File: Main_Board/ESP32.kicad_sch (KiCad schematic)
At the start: 11 parts, among them J1 RESET, J2 MAIN_UART, U1 ESP32-S3-MINI-1U

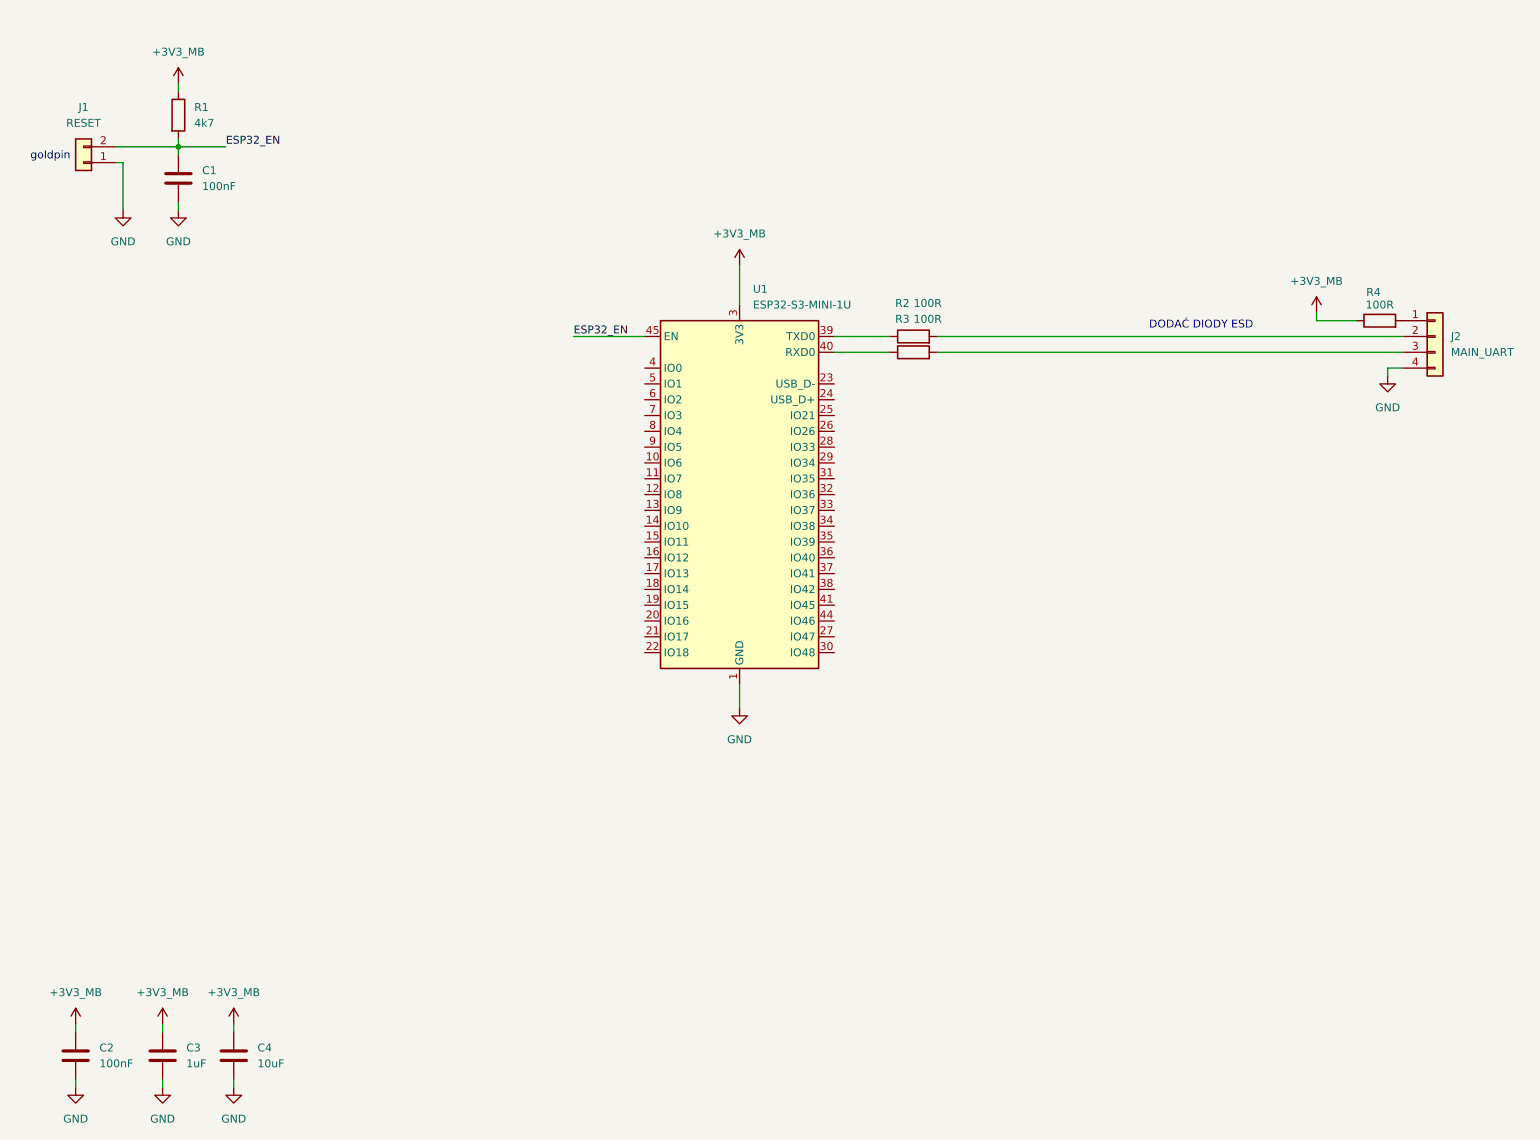
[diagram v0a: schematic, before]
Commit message: PSU Ready + ESP32 advanced
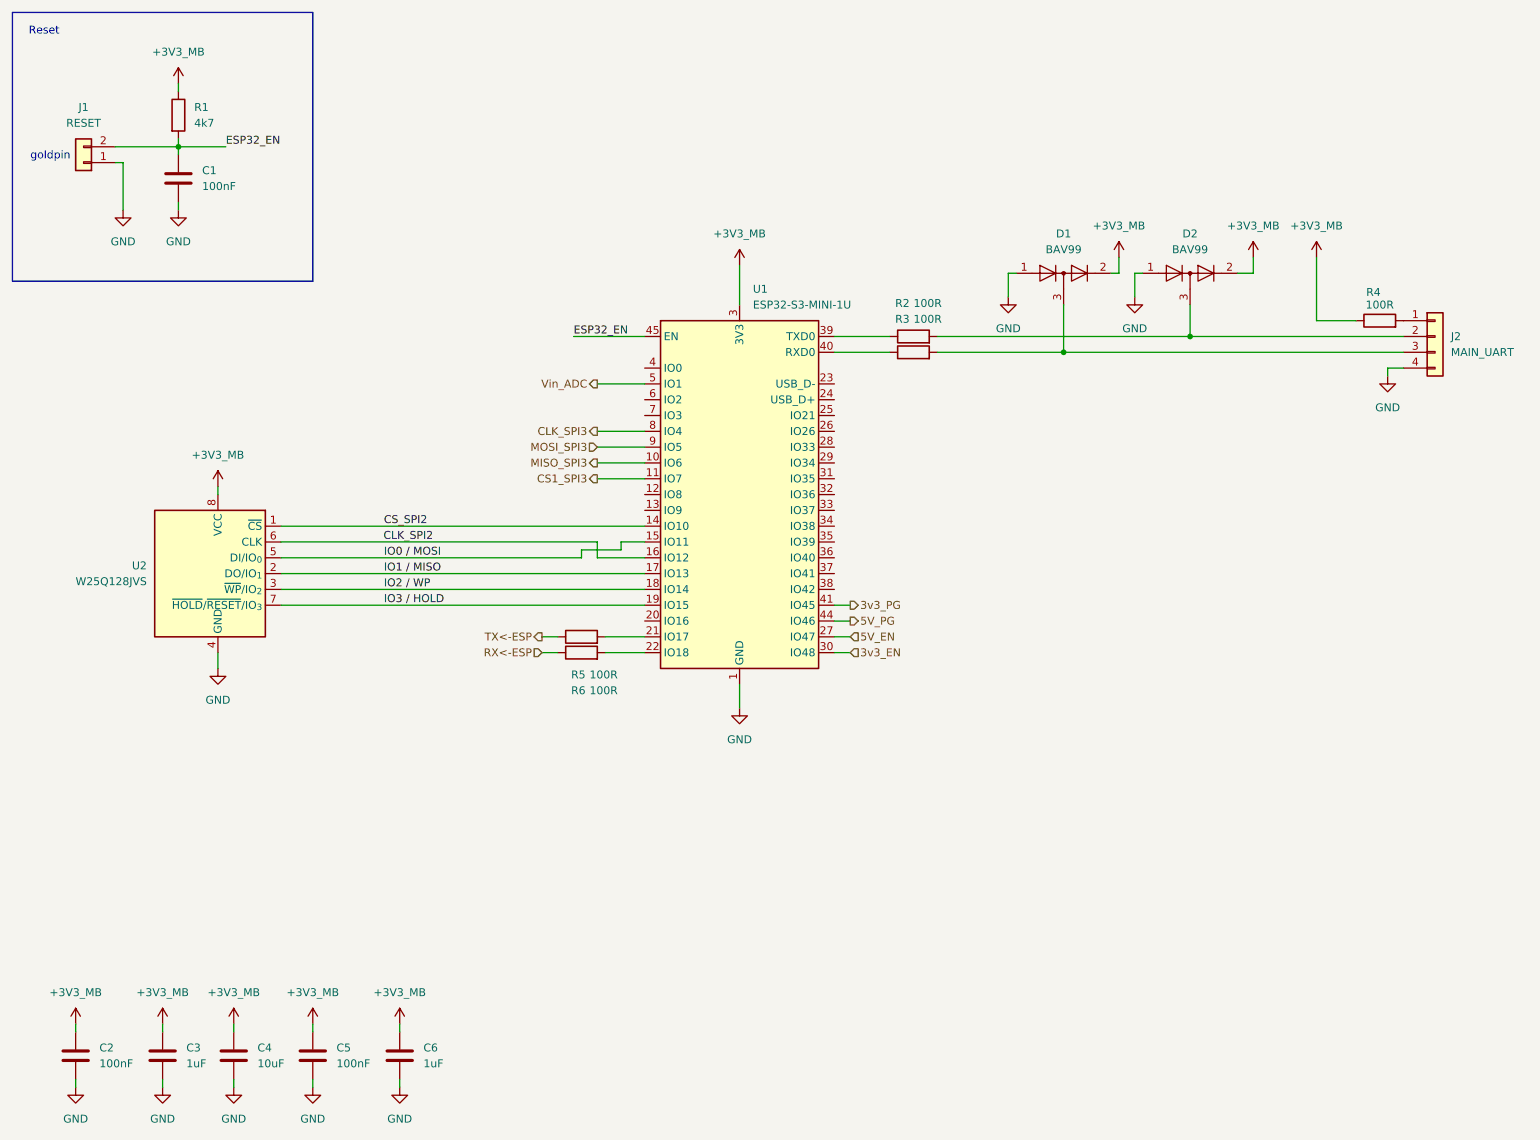
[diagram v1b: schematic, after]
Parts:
- added C5: 100nF, symbol Device:C
- added C6: 1uF, symbol Device:C
- added D1, D2: BAV99, Package_TO_SOT_SMD:SOT-23, symbol Diode:BAV99
- added R5, R6: 100R, symbol Device:R
- added U2: W25Q128JVS, Package_SO:SOIC-8_5.3x5.3mm_P1.27mm, symbol Memory_Flash:W25Q128JVS
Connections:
- net +3V3_MB: now also C5.1, C6.1, D1.2 (A), D2.2 (A), U2.8 (VCC)
- net GND: now also C5.2, C6.2, D1.1 (K), D2.1 (K), U2.4 (GND)
- net at J2.2 (Pin_2), R2.2: now also D2.3 (K)
- net MISO_SPI3: now reaches U1.10 (IO6)
- net CS1_SPI3: now reaches U1.11 (IO7)
- net CS_SPI2: now reaches U1.14 (IO10)
- net CS_SPI2: now also U2.1 (~{CS})
- net IO0 / MOSI: now reaches U1.15 (IO11)
- net IO0 / MOSI: now also U2.5 (DI/IO_{0})
- net CLK_SPI2: now reaches U1.16 (IO12)
- net CLK_SPI2: now also U2.6 (CLK)
- net IO1 / MISO: now reaches U1.17 (IO13)
- net IO1 / MISO: now also U2.2 (DO/IO_{1})
- net IO2 / WP: now reaches U1.18 (IO14)
- net IO2 / WP: now also U2.3 (~{WP}/IO_{2})
- net IO3 / HOLD: now reaches U1.19 (IO15)
- net IO3 / HOLD: now also U2.7 (~{HOLD}/~{RESET}/IO_{3})
- net at U1.21 (IO17): now also R5.2
- net at U1.22 (IO18): now also R6.2
- net 5V_EN: now reaches U1.27 (IO47)
- net 3v3_EN: now reaches U1.30 (IO48)
- net 3v3_PG: now reaches U1.41 (IO45)
- net 5V_PG: now reaches U1.44 (IO46)
- net Vin_ADC: now reaches U1.5 (IO1)
- net CLK_SPI3: now reaches U1.8 (IO4)
- net MOSI_SPI3: now reaches U1.9 (IO5)
- net at J2.3 (Pin_3), R3.2: now also D1.3 (K)
- new net RX<-ESP: R6.1
- new net TX<-ESP: R5.1
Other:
- note added: "Reset"
- note removed: "DODAĆ DIODY ESD"

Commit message: Input Protection
Irlm is left to be calculated
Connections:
- no-connect marks 0 -> 2
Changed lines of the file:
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@@
 		(color 0 0 0 0)
+	)
+	(no_connect
+		(at 146.05 77.47)
+	)
+	(no_connect
+		(at 146.05 74.93)
 	)
 	(wire

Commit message: RS485 Transciever + Input Protection fix
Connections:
- net RSDIR: now reaches U1.25 (IO21)
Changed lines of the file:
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@@
+	(wire
+		(pts
+			(xy 148.59 80.01) (xy 146.05 80.01)
+		)
+		(stroke
+			(width 0)
+			(type default)
+		)
+	)
 	(wire
 		(pts
@@
 		(effects
 			(font
+				(size 1.27 1.27)
+			)
+			(justify left)
+		)
+	)
+	(hierarchical_label "RSDIR"
+		(shape input)
+		(at 148.59 80.01 0)
+		(effects
+			(font

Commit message: Aesthetics/cleanup
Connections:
- net RSDIR renamed MODULE_BUS_DIR
- net RX<-ESP renamed MODULE_BUS_RX
- net TX<-ESP renamed MODULE_BUS_TX
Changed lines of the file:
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@@
 		)
 	)
-	(hierarchical_label "RSDIR"
+	(hierarchical_label "MODULE_BUS_DIR"
 		(shape input)
 		(at 148.59 80.01 0)
@@
 		)
 	)
-	(hierarchical_label "RX<-ESP"
+	(hierarchical_label "MODULE_BUS_RX"
 		(shape input)
 		(at 99.06 118.11 180)
@@
 		)
 	)
-	(hierarchical_label "TX<-ESP"
+	(hierarchical_label "MODULE_BUS_TX"
 		(shape output)
 		(at 99.06 115.57 180)

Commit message: add external obrds interfaces
Todo pyro chanells
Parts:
- added Q1: 2N7002, Package_TO_SOT_SMD:SOT-23, symbol Transistor_FET:2N7002
- added R32: 4k7, symbol Device:R
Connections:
- net ESP32_EN: now also Q1.3 (D)
- net GND: now also Q1.2 (S), R32.2
- net MODULE_BUS_DIR: now also U1.20 (IO16); no longer U1.25 (IO21)
- new net RST: Q1.1 (G), R32.1
- new net SYNC: U1.25 (IO21)

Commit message: Add buzzer, Add LED, ADD R&D jumper
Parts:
- added R5, R6, R7, R8: 100R, symbol Device:R
- renumbered C2 to C1, C3 to C2, C1 to C3, R32 to R1, R3 to R10, R4 to R11, R1 to R2, R5 to R3, R6 to R4, R2 to R9, U2 to U1, U1 to U2
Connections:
- net at U2.35 (IO39): now also R5.1
- net at U2.36 (IO40): now also R6.1
- net at U2.37 (IO41): now also R7.1
- net at U2.38 (IO42): now also R8.1
- new net BUZZER: R6.2
- new net LED: R5.2
- new net Piro1: R7.2
- new net Piro2: R8.2

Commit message: ADD footprints
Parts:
- C1, C2, C3, C4, C5, C6: footprint (none) -> Capacitor_SMD:C_0603_1608Metric
- J1: footprint (none) -> Connector_PinHeader_2.54mm:PinHeader_1x02_P2.54mm_Vertical
- J2: footprint (none) -> Connector_PinHeader_2.54mm:PinHeader_1x04_P2.54mm_Horizontal
- R1, R10, R11, R2, R3, R4, R5, R6, R7, R8, R9: footprint (none) -> Resistor_SMD:R_0603_1608Metric
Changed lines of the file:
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@@
 			)
 		)
-		(property "Footprint" ""
+		(property "Footprint" "Resistor_SMD:R_0603_1608Metric"
 			(at 233.68 66.548 90)
 			(hide yes)
@@
 			)
 		)
-		(property "Footprint" ""
+		(property "Footprint" "Capacitor_SMD:C_0603_1608Metric"
 			(at 41.6052 45.72 0)
 			(hide yes)
@@
 			)
 		)
-		(property "Footprint" ""
+		(property "Footprint" "Resistor_SMD:R_0603_1608Metric"
 			(at 38.862 31.75 90)
 			(hide yes)
@@
 			)
 		)
-		(property "Footprint" ""
+		(property "Footprint" "Resistor_SMD:R_0603_1608Metric"
 			(at 158.75 69.088 90)
 			(hide yes)
@@
 			)
 		)
-		(property "Footprint" ""
+		(property "Footprint" "Capacitor_SMD:C_0603_1608Metric"
 			(at 50.4952 186.69 0)
 			(hide yes)
@@
 			)
 		)
-		(property "Footprint" ""
+		(property "Footprint" "Resistor_SMD:R_0603_1608Metric"
 			(at 23.622 66.04 90)
 			(hide yes)
@@
 			)
 		)
-		(property "Footprint" ""
+		(property "Footprint" "Capacitor_SMD:C_0603_1608Metric"
 			(at 25.0952 186.69 0)
 			(hide yes)
@@
 			)
 		)
-		(property "Footprint" ""
+		(property "Footprint" "Capacitor_SMD:C_0603_1608Metric"
 			(at 77.1652 186.69 0)
 			(hide yes)
@@
 			)
 		)
-		(property "Footprint" ""
+		(property "Footprint" "Resistor_SMD:R_0603_1608Metric"
 			(at 105.41 119.888 90)
 			(hide yes)
@@
 			)
 		)
-		(property "Footprint" ""
+		(property "Footprint" "Resistor_SMD:R_0603_1608Metric"
 			(at 152.4 104.648 90)
 			(hide yes)
@@
 			)
 		)
-		(property "Footprint" ""
+		(property "Footprint" "Resistor_SMD:R_0603_1608Metric"
 			(at 152.4 107.188 90)
 			(hide yes)
@@
 			)
 		)
-		(property "Footprint" ""
+		(property "Footprint" "Resistor_SMD:R_0603_1608Metric"
 			(at 152.4 109.728 90)
 			(hide yes)
@@
 			)
 		)
-		(property "Footprint" ""
+		(property "Footprint" "Resistor_SMD:R_0603_1608Metric"
 			(at 105.41 117.348 90)
 			(hide yes)
@@
 			)
 		)
-		(property "Footprint" ""
+		(property "Footprint" "Capacitor_SMD:C_0603_1608Metric"
 			(at 39.0652 186.69 0)
 			(hide yes)
@@
 			)
 		)
-		(property "Footprint" ""
+		(property "Footprint" "Resistor_SMD:R_0603_1608Metric"
 			(at 152.4 102.108 90)
 			(hide yes)
@@
 			)
 		)
-		(property "Footprint" ""
+		(property "Footprint" "Connector_PinHeader_2.54mm:PinHeader_1x02_P2.54mm_Vertical"
 			(at 25.4 39.37 0)
 			(hide yes)
@@
 			)
 		)
-		(property "Footprint" ""
+		(property "Footprint" "Connector_PinHeader_2.54mm:PinHeader_1x04_P2.54mm_Horizontal"
 			(at 242.57 67.31 0)
 			(hide yes)
@@
 			)
 		)
-		(property "Footprint" ""
+		(property "Footprint" "Resistor_SMD:R_0603_1608Metric"
 			(at 158.75 71.628 90)
 			(hide yes)
@@
 			)
 		)
-		(property "Footprint" ""
+		(property "Footprint" "Capacitor_SMD:C_0603_1608Metric"
 			(at 63.1952 186.69 0)
 			(hide yes)
